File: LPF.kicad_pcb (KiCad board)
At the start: 4 copper layers, 100 x 100 mm, 139 parts, among them J1 Conn_02x05_Counter_Clockwise, P1 SMA, P3 SMA, P4 SMA

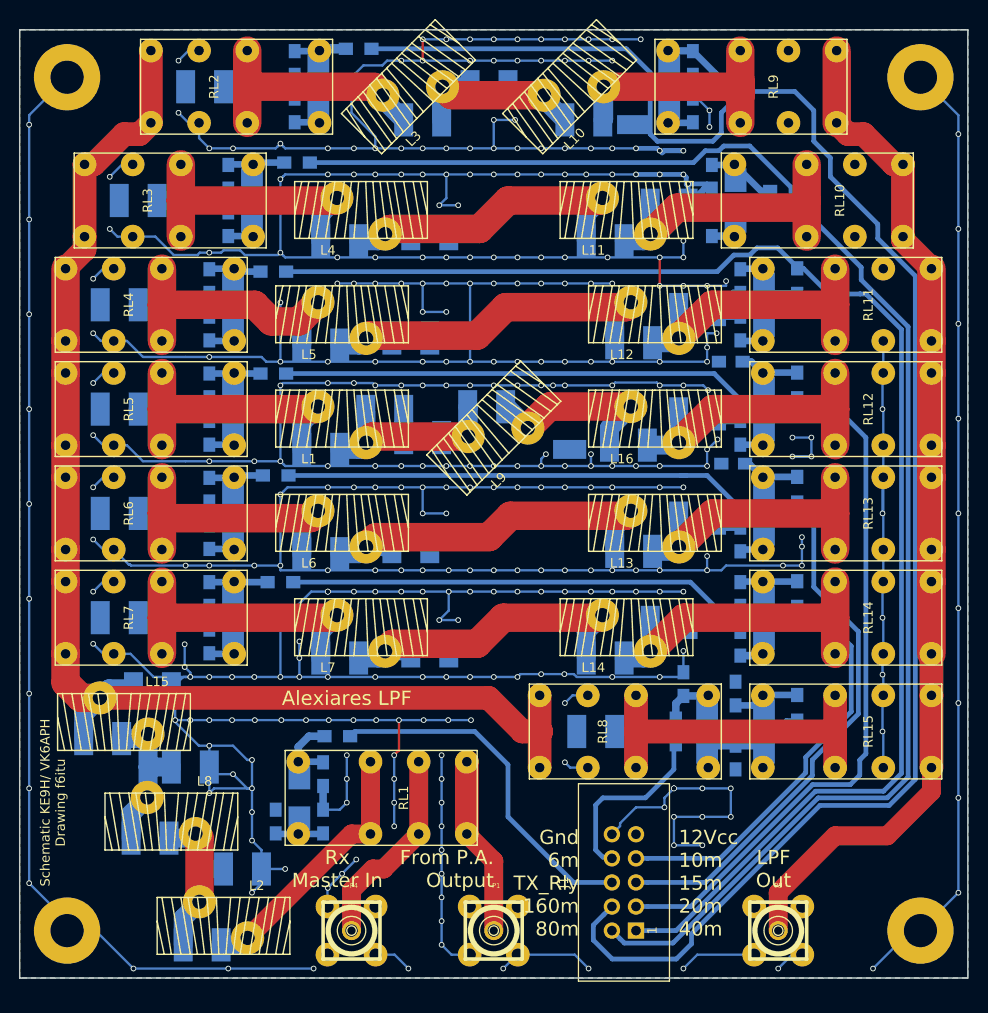
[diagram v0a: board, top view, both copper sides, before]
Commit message: new routing after ATC100B change, RTM2
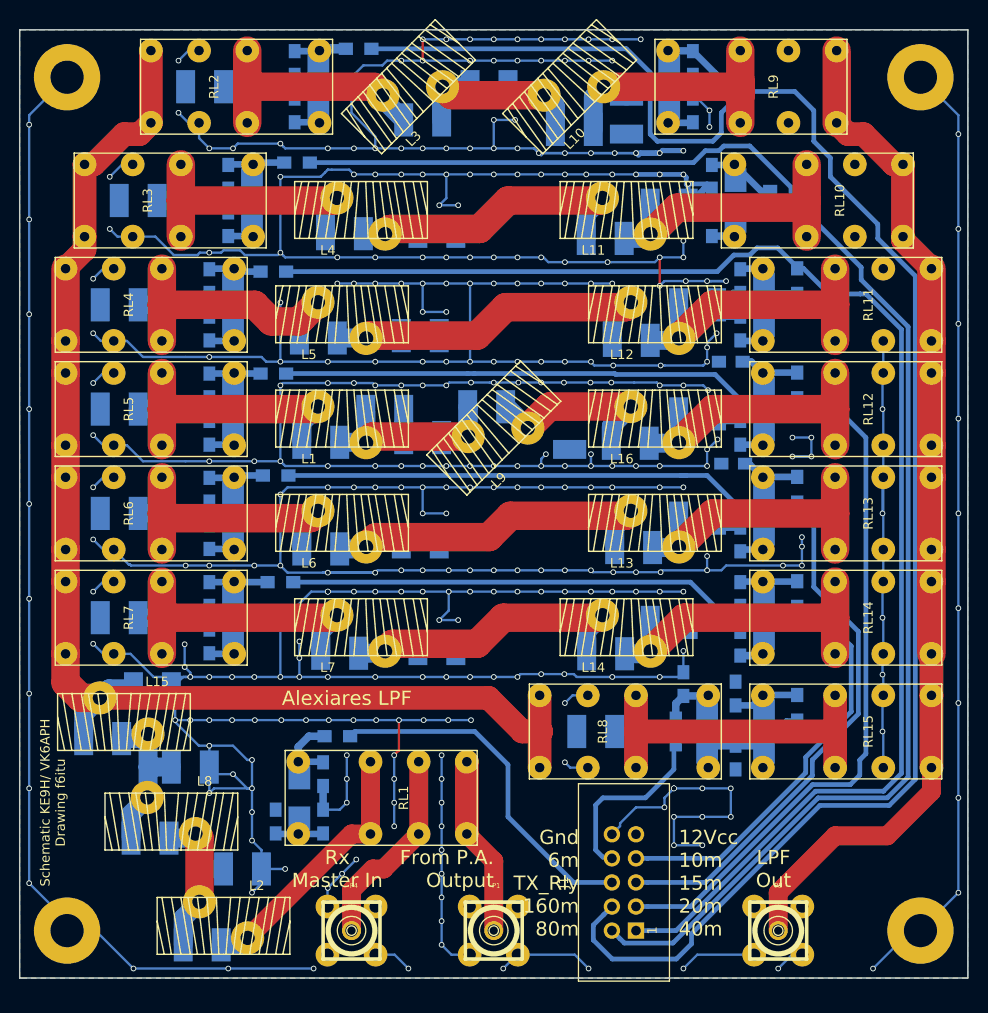
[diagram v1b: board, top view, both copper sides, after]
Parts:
- moved C39 1.41 mm to (113.5, 55.5)
- moved C46 1.25 mm to (119.0, 54.0)
- moved C36 1.12 mm to (97.2, 99.0)
- moved C34 1.03 mm to (97.2, 77.2)
- moved C26 0.90 mm to (89.2, 66.5)
- moved C27 0.79 mm to (86.5, 77.5)
- moved C33 0.79 mm to (99.0, 66.2)
- moved C37 0.79 mm to (99.0, 110.2)
- moved C16 0.75 mm to (86.8, 88.5)
- moved C28 0.50 mm to (86.8, 99.8)
- moved C29 0.50 mm to (88.8, 110.8)
- moved C48 0.50 mm to (126.5, 74.0)
- moved C44 0.45 mm to (116.8, 110.8)
- moved C43 0.40 mm to (119.8, 99.6)
- moved C41 0.35 mm to (119.5, 77.8)
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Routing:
- net 160m: track 166.6 -> 181.3 mm
- net GND: track 1308.3 -> 1313.1 mm, vias 338 -> 337
- net Net-(C27-Pad2): track 40.3 -> 41.6 mm
- net Net-(C39-Pad2): track 30.6 -> 31.7 mm
- net Net-(C20-Pad2): track 39.5 -> 38.6 mm
- net Net-(C51-Pad2): track 32.7 -> 31.8 mm
- net Net-(C43-Pad2): track 32.2 -> 31.4 mm
- net Net-(C11-Pad2): track 39.5 -> 38.8 mm
- net Net-(C28-Pad2): track 40.3 -> 41.0 mm
- net Net-(C41-Pad2): track 31.6 -> 32.3 mm
- net Net-(C21-Pad2): track 41.1 -> 40.4 mm
- net Net-(C25-Pad2): track 21.0 -> 21.6 mm
- net Net-(C23-Pad2): track 41.6 -> 41.1 mm
- net Net-(C22-Pad2): track 40.1 -> 39.6 mm

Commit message: minor routing changes, via added
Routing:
- added copper zone on In2.Cu, net +12V
- added copper zone on In1.Cu, net GND
- removed copper zone on In1.Cu, net +12V
- removed copper zone on In2.Cu, net GND

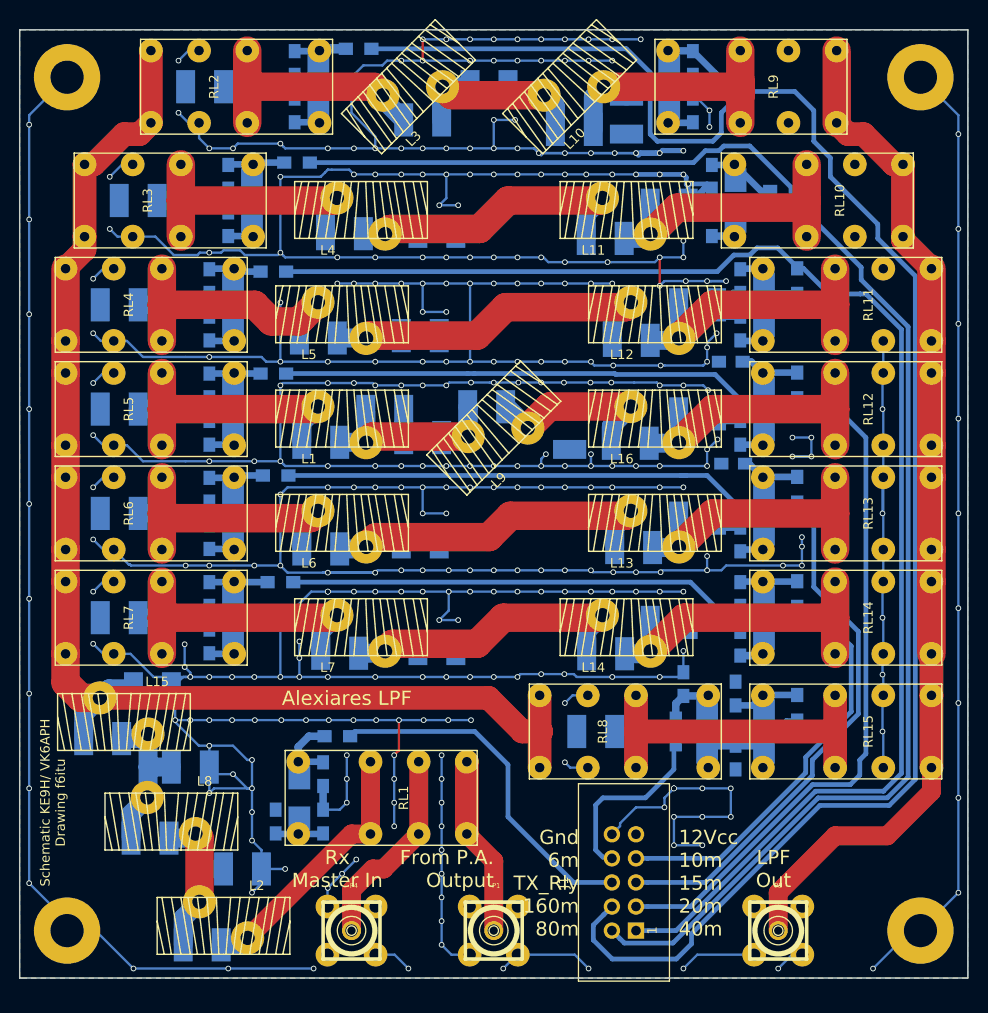
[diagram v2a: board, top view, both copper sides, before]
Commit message: add forbiden zone under bypass power caps
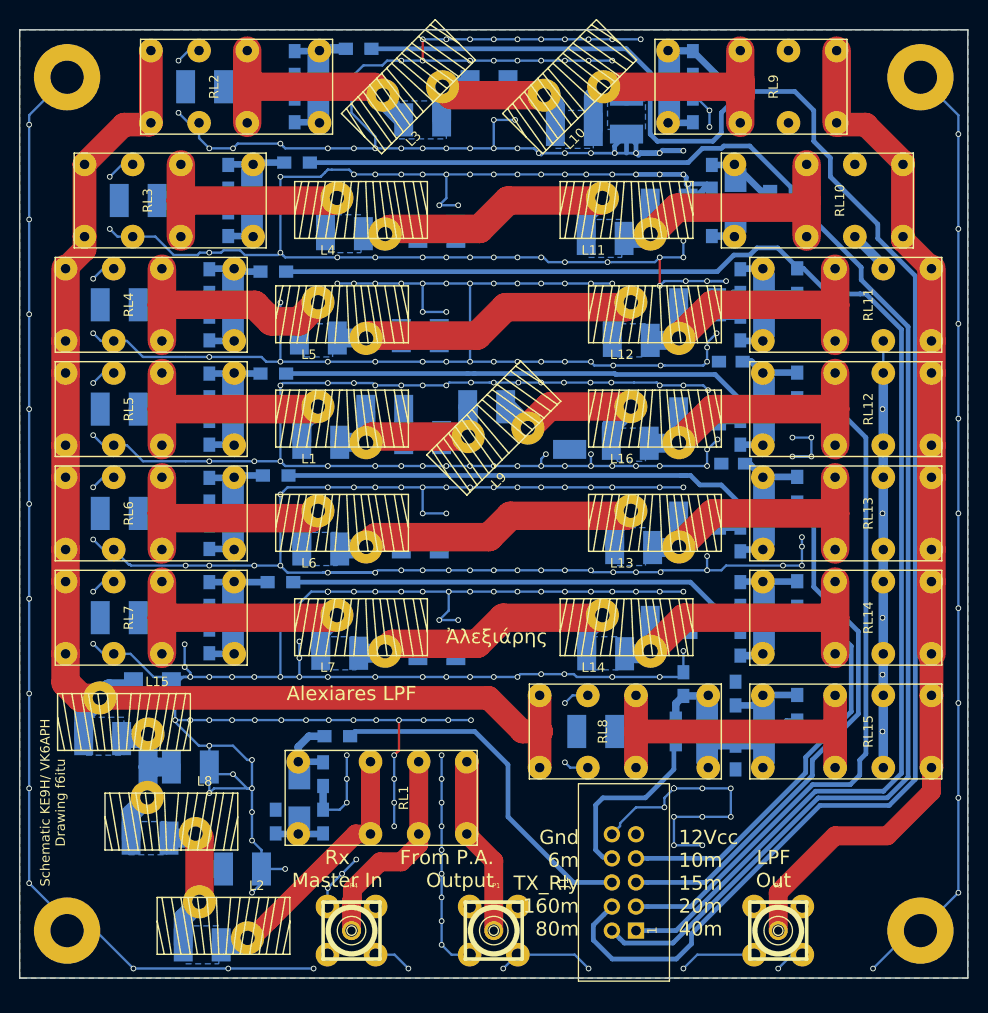
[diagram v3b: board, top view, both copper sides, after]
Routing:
- net GND: track 1313.1 -> 1404.0 mm
- net Net-(C17-Pad1): track 28.2 -> 31.9 mm
- net Net-(P4-Pad1): track 21.4 -> 22.1 mm
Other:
- board text added: "Ἀλεξιάρης"

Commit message: trace cleaning, SMA edge added, main connector rotated
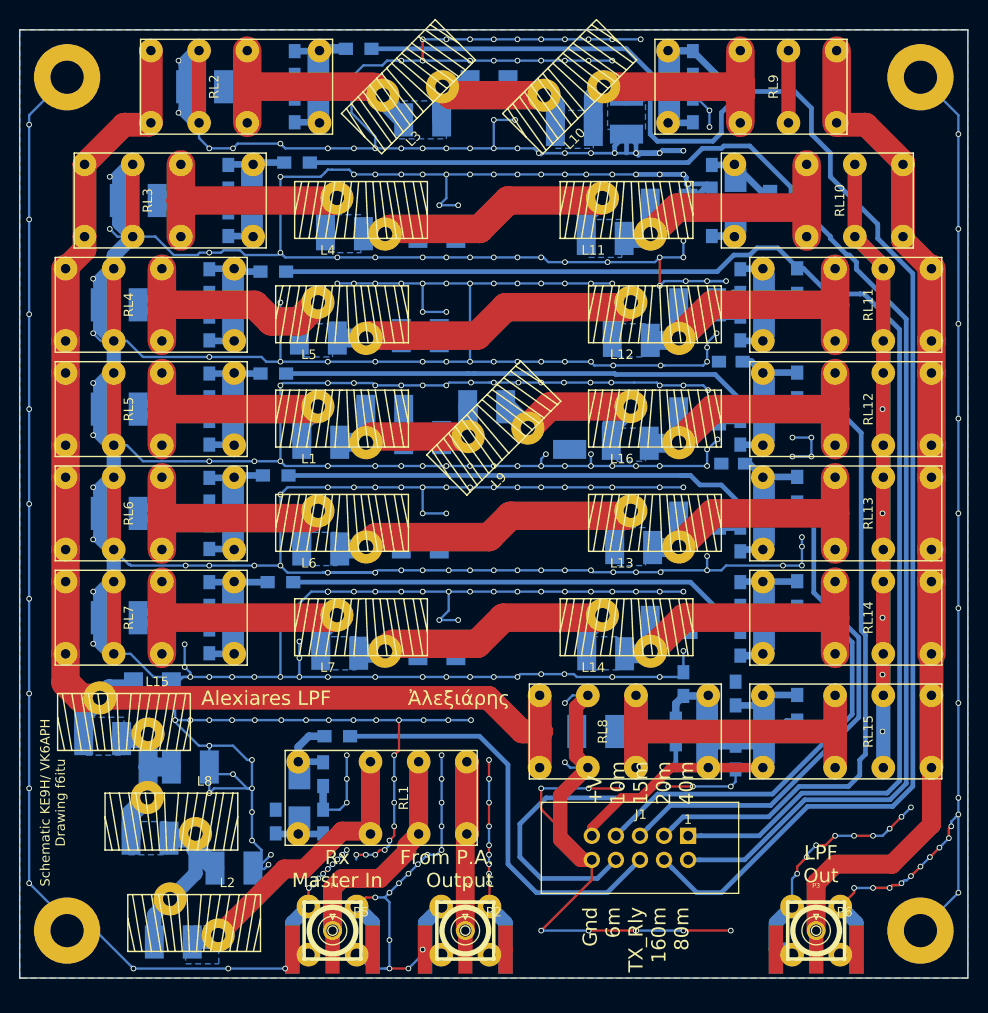
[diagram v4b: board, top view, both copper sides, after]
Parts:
- added P2: SMA, Connector_Coaxial:SMA_Amphenol_132289_EdgeMount, F.Cu at (102.0, 142.0)
- added P5: SMA, Connector_Coaxial:SMA_Amphenol_132289_EdgeMount, F.Cu at (88.0, 142.0)
- added P6: SMA, Connector_Coaxial:SMA_Amphenol_132289_EdgeMount, F.Cu at (139.0, 142.0)
- moved J1 11.4 mm to (125.5, 130.0), turned to 180 degrees
- moved P3 4.00 mm to (139.0, 140.0)
- moved L2 3.11 mm to (73.4, 139.2)
- moved C17 3.06 mm to (71.2, 141.2)
- moved P1 3.00 mm to (102.0, 140.0)
- moved P4 2.00 mm to (88.0, 140.0)
- moved C24 0.91 mm to (77.6, 133.4)
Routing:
- net GND: track 1404.0 -> 1722.1 mm, vias 337 -> 379
- net +12V: track 70.2 -> 91.7 mm
- net 6m_Bypass: track 33.1 -> 50.6 mm
- net 160m: track 181.3 -> 166.7 mm
- net 80m: track 159.7 -> 147.7 mm
- net 40m: track 151.2 -> 141.7 mm
- net TX_RX_RLY: track 37.6 -> 45.0 mm
- net 30/20m: track 130.3 -> 124.2 mm
- net Net-(C17-Pad2): track 25.9 -> 20.7 mm
- net Net-(P4-Pad1): track 22.1 -> 25.9 mm
- net 17/15m: track 113.3 -> 110.1 mm
- net 12/10m: track 99.7 -> 100.5 mm
- net Net-(P1-Pad1): track 19.2 -> 19.9 mm
- net Net-(P3-Pad1): track 108.6 -> 109.2 mm
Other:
- board text added: "+V 10m 15m 20m 40m"
- board text added: "12 Vcc 10m 15m 20m 40m"
- board text added: "Gnd 6m-BP TX_Rly 160m 80m"
- board text removed: "12Vcc 10m 15m 20m 40m"
- board text removed: "Gnd 6m-ByPass TX_Rly 160m 80m"

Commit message: changed sma footprint, gerber done
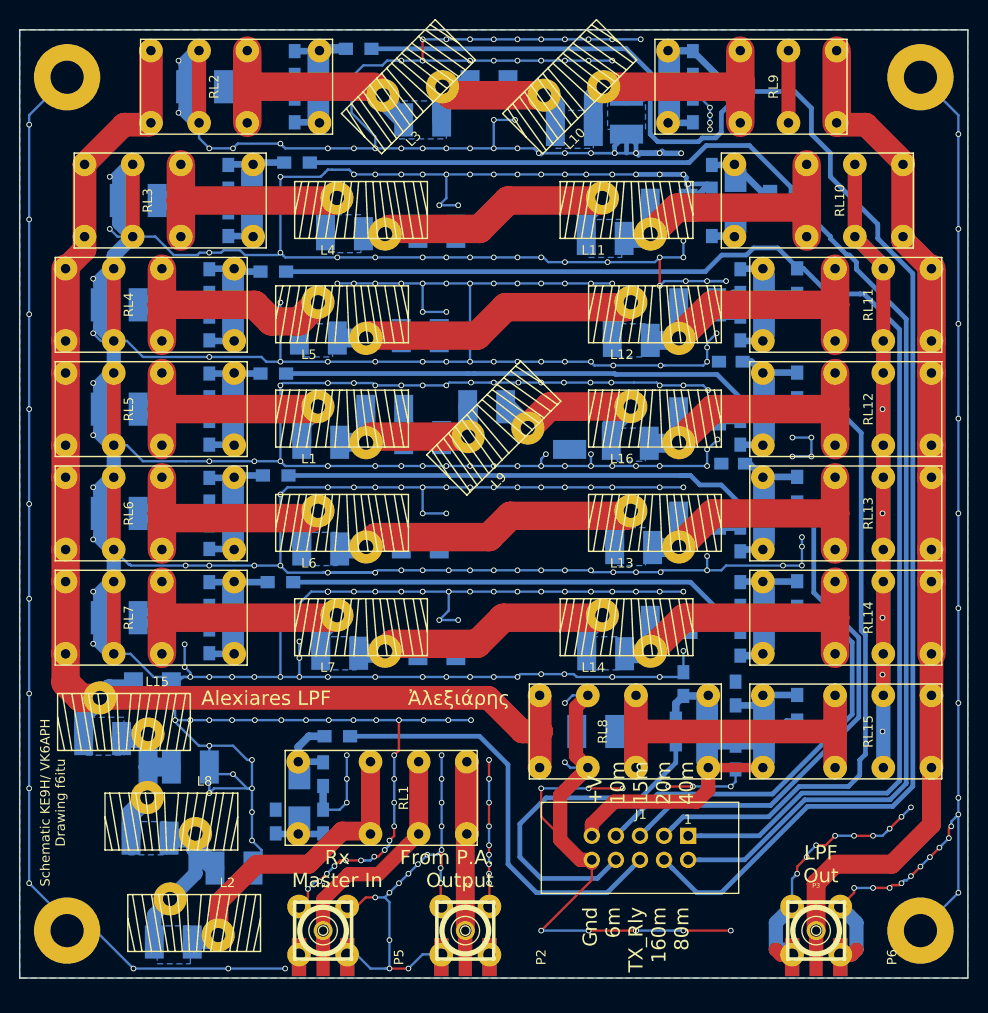
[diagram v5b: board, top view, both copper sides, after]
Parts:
- P2, P5, P6: footprint Connector_Coaxial:SMA_Amphenol_132289_EdgeMount -> SMA_PINS:SMA_EDGE_NRW
- moved P5 1.28 mm to (87.0, 142.8)
- moved P4 1.00 mm to (87.0, 140.0)
- moved P2 0.80 mm to (102.0, 142.8)
- moved P6 0.80 mm to (139.0, 142.8)
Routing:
- net GND: track 1722.1 -> 1697.0 mm, vias 379 -> 375
- net Net-(C17-Pad1): track 31.6 -> 33.6 mm
- net +12V: track 91.7 -> 93.3 mm

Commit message: stitching and new gerber
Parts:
- added REF**: via, via:via, F.Cu at (134.0, 144.0)
- added REF**: via, via:via, F.Cu at (125.0, 144.0)
- added REF**: via, via:via, F.Cu at (119.0, 141.0)
- added REF**: via, via:via, F.Cu at (118.0, 141.0)
- added REF**: via, via:via, F.Cu at (117.0, 141.0)
- added REF**: via, via:via, F.Cu at (116.0, 141.0)
- added REF**: via, via:via, F.Cu at (115.0, 141.0)
- added REF**: via, via:via, F.Cu at (114.0, 141.0)
- added REF**: via, via:via, F.Cu at (113.0, 141.0)
- added REF**: via, via:via, F.Cu at (112.0, 141.0)
- added REF**: via, via:via, F.Cu at (111.0, 141.0)
- added REF**: via, via:via, F.Cu at (110.0, 141.0)
- added REF**: via, via:via, F.Cu at (124.0, 144.0)
- added REF**: via, via:via, F.Cu at (109.0, 141.0)
- added REF**: via, via:via, F.Cu at (108.0, 141.0)
- added REF**: via, via:via, F.Cu at (107.0, 141.0)
- added REF**: via, via:via, F.Cu at (134.0, 140.0)
- added REF**: via, via:via, F.Cu at (133.0, 140.0)
- added REF**: via, via:via, F.Cu at (132.0, 140.0)
- added REF**: via, via:via, F.Cu at (131.0, 140.0)
- added REF**: via, via:via, F.Cu at (130.0, 140.0)
- added REF**: via, via:via, F.Cu at (129.0, 140.0)
- added REF**: via, via:via, F.Cu at (128.0, 140.0)
- added REF**: via, via:via, F.Cu at (123.0, 144.0)
- added REF**: via, via:via, F.Cu at (127.0, 140.0)
- added REF**: via, via:via, F.Cu at (126.0, 140.0)
- added REF**: via, via:via, F.Cu at (125.0, 140.0)
- added REF**: via, via:via, F.Cu at (124.0, 140.0)
- added REF**: via, via:via, F.Cu at (123.0, 140.0)
- added REF**: via, via:via, F.Cu at (122.0, 140.0)
- added REF**: via, via:via, F.Cu at (121.0, 140.0)
- added REF**: via, via:via, F.Cu at (120.0, 140.0)
- added REF**: via, via:via, F.Cu at (119.0, 140.0)
- added REF**: via, via:via, F.Cu at (118.0, 140.0)
- added REF**: via, via:via, F.Cu at (122.0, 144.0)
- added REF**: via, via:via, F.Cu at (117.0, 140.0)
- added REF**: via, via:via, F.Cu at (116.0, 140.0)
- added REF**: via, via:via, F.Cu at (115.0, 140.0)
- added REF**: via, via:via, F.Cu at (114.0, 140.0)
- added REF**: via, via:via, F.Cu at (113.0, 140.0)
- added REF**: via, via:via, F.Cu at (112.0, 140.0)
- added REF**: via, via:via, F.Cu at (111.0, 140.0)
- added REF**: via, via:via, F.Cu at (110.0, 140.0)
- added REF**: via, via:via, F.Cu at (109.0, 140.0)
- added REF**: via, via:via, F.Cu at (108.0, 140.0)
- added REF**: via, via:via, F.Cu at (121.0, 144.0)
- added REF**: via, via:via, F.Cu at (107.0, 140.0)
- added REF**: via, via:via, F.Cu at (134.0, 139.0)
- added REF**: via, via:via, F.Cu at (133.0, 139.0)
- added REF**: via, via:via, F.Cu at (132.0, 139.0)
- added REF**: via, via:via, F.Cu at (131.0, 139.0)
- added REF**: via, via:via, F.Cu at (130.0, 139.0)
- added REF**: via, via:via, F.Cu at (129.0, 139.0)
- added REF**: via, via:via, F.Cu at (128.0, 139.0)
- added REF**: via, via:via, F.Cu at (127.0, 139.0)
- added REF**: via, via:via, F.Cu at (126.0, 139.0)
- added REF**: via, via:via, F.Cu at (120.0, 144.0)
- added REF**: via, via:via, F.Cu at (125.0, 139.0)
- added REF**: via, via:via, F.Cu at (124.0, 139.0)
- added REF**: via, via:via, F.Cu at (123.0, 139.0)
- added REF**: via, via:via, F.Cu at (122.0, 139.0)
- added REF**: via, via:via, F.Cu at (121.0, 139.0)
- added REF**: via, via:via, F.Cu at (120.0, 139.0)
- added REF**: via, via:via, F.Cu at (119.0, 139.0)
- added REF**: via, via:via, F.Cu at (118.0, 139.0)
- added REF**: via, via:via, F.Cu at (117.0, 139.0)
- added REF**: via, via:via, F.Cu at (116.0, 139.0)
- added REF**: via, via:via, F.Cu at (119.0, 144.0)
- added REF**: via, via:via, F.Cu at (115.0, 139.0)
- added REF**: via, via:via, F.Cu at (114.0, 139.0)
- added REF**: via, via:via, F.Cu at (113.0, 139.0)
- added REF**: via, via:via, F.Cu at (112.0, 139.0)
- added REF**: via, via:via, F.Cu at (111.0, 139.0)
- added REF**: via, via:via, F.Cu at (110.0, 139.0)
- added REF**: via, via:via, F.Cu at (109.0, 139.0)
- added REF**: via, via:via, F.Cu at (108.0, 139.0)
- added REF**: via, via:via, F.Cu at (107.0, 139.0)
- added REF**: via, via:via, F.Cu at (134.0, 138.0)
- added REF**: via, via:via, F.Cu at (118.0, 144.0)
- added REF**: via, via:via, F.Cu at (133.0, 138.0)
- added REF**: via, via:via, F.Cu at (132.0, 138.0)
- added REF**: via, via:via, F.Cu at (131.0, 138.0)
- added REF**: via, via:via, F.Cu at (130.0, 138.0)
- added REF**: via, via:via, F.Cu at (129.0, 138.0)
- added REF**: via, via:via, F.Cu at (128.0, 138.0)
- added REF**: via, via:via, F.Cu at (127.0, 138.0)
- added REF**: via, via:via, F.Cu at (126.0, 138.0)
- added REF**: via, via:via, F.Cu at (125.0, 138.0)
- added REF**: via, via:via, F.Cu at (124.0, 138.0)
- added REF**: via, via:via, F.Cu at (117.0, 144.0)
- added REF**: via, via:via, F.Cu at (123.0, 138.0)
- added REF**: via, via:via, F.Cu at (122.0, 138.0)
- added REF**: via, via:via, F.Cu at (121.0, 138.0)
- added REF**: via, via:via, F.Cu at (120.0, 138.0)
- added REF**: via, via:via, F.Cu at (119.0, 138.0)
- added REF**: via, via:via, F.Cu at (118.0, 138.0)
- added REF**: via, via:via, F.Cu at (117.0, 138.0)
- added REF**: via, via:via, F.Cu at (116.0, 138.0)
- added REF**: via, via:via, F.Cu at (115.0, 138.0)
- added REF**: via, via:via, F.Cu at (114.0, 138.0)
- added REF**: via, via:via, F.Cu at (116.0, 144.0)
- added REF**: via, via:via, F.Cu at (113.0, 138.0)
- added REF**: via, via:via, F.Cu at (112.0, 138.0)
- added REF**: via, via:via, F.Cu at (111.0, 138.0)
- added REF**: via, via:via, F.Cu at (110.0, 138.0)
- added REF**: via, via:via, F.Cu at (109.0, 138.0)
- added REF**: via, via:via, F.Cu at (108.0, 138.0)
- added REF**: via, via:via, F.Cu at (107.0, 138.0)
- added REF**: via, via:via, F.Cu at (154.0, 136.0)
- added REF**: via, via:via, F.Cu at (154.0, 135.0)
- added REF**: via, via:via, F.Cu at (154.0, 134.0)
- added REF**: via, via:via, F.Cu at (133.0, 144.0)
- added REF**: via, via:via, F.Cu at (115.0, 144.0)
- added REF**: via, via:via, F.Cu at (154.0, 133.0)
- added REF**: via, via:via, F.Cu at (154.0, 132.0)
- added REF**: via, via:via, F.Cu at (154.0, 131.0)
- added REF**: via, via:via, F.Cu at (154.0, 130.0)
- added REF**: via, via:via, F.Cu at (154.0, 129.0)
- added REF**: via, via:via, F.Cu at (154.0, 128.0)
- added REF**: via, via:via, F.Cu at (154.0, 127.0)
- added REF**: via, via:via, F.Cu at (154.0, 126.0)
- added REF**: via, via:via, F.Cu at (154.0, 125.0)
- added REF**: via, via:via, F.Cu at (154.0, 124.0)
- added REF**: via, via:via, F.Cu at (114.0, 144.0)
- added REF**: via, via:via, F.Cu at (154.0, 123.0)
- added REF**: via, via:via, F.Cu at (154.0, 122.0)
- added REF**: via, via:via, F.Cu at (154.0, 121.0)
- added REF**: via, via:via, F.Cu at (154.0, 120.0)
- added REF**: via, via:via, F.Cu at (154.0, 119.0)
- added REF**: via, via:via, F.Cu at (154.0, 118.0)
- added REF**: via, via:via, F.Cu at (154.0, 117.0)
- added REF**: via, via:via, F.Cu at (154.0, 116.0)
- added REF**: via, via:via, F.Cu at (154.0, 115.0)
- added REF**: via, via:via, F.Cu at (154.0, 114.0)
- added REF**: via, via:via, F.Cu at (113.0, 144.0)
- added REF**: via, via:via, F.Cu at (154.0, 113.0)
- added REF**: via, via:via, F.Cu at (154.0, 112.0)
- added REF**: via, via:via, F.Cu at (154.0, 111.0)
- added REF**: via, via:via, F.Cu at (154.0, 110.0)
- added REF**: via, via:via, F.Cu at (154.0, 109.0)
- added REF**: via, via:via, F.Cu at (154.0, 108.0)
- added REF**: via, via:via, F.Cu at (154.0, 107.0)
- added REF**: via, via:via, F.Cu at (154.0, 106.0)
- added REF**: via, via:via, F.Cu at (154.0, 105.0)
- added REF**: via, via:via, F.Cu at (154.0, 104.0)
- added REF**: via, via:via, F.Cu at (112.0, 144.0)
- added REF**: via, via:via, F.Cu at (154.0, 103.0)
- added REF**: via, via:via, F.Cu at (154.0, 102.0)
- added REF**: via, via:via, F.Cu at (154.0, 101.0)
- added REF**: via, via:via, F.Cu at (154.0, 100.0)
- added REF**: via, via:via, F.Cu at (154.0, 99.0)
- added REF**: via, via:via, F.Cu at (154.0, 98.0)
- added REF**: via, via:via, F.Cu at (154.0, 97.0)
- added REF**: via, via:via, F.Cu at (154.0, 96.0)
- added REF**: via, via:via, F.Cu at (154.0, 95.0)
- added REF**: via, via:via, F.Cu at (154.0, 94.0)
- added REF**: via, via:via, F.Cu at (111.0, 144.0)
- added REF**: via, via:via, F.Cu at (154.0, 93.0)
- added REF**: via, via:via, F.Cu at (154.0, 92.0)
- added REF**: via, via:via, F.Cu at (154.0, 91.0)
- added REF**: via, via:via, F.Cu at (154.0, 90.0)
- added REF**: via, via:via, F.Cu at (154.0, 89.0)
- added REF**: via, via:via, F.Cu at (154.0, 88.0)
- added REF**: via, via:via, F.Cu at (154.0, 87.0)
- added REF**: via, via:via, F.Cu at (154.0, 86.0)
- added REF**: via, via:via, F.Cu at (154.0, 85.0)
- added REF**: via, via:via, F.Cu at (154.0, 84.0)
- added REF**: via, via:via, F.Cu at (110.0, 144.0)
- added REF**: via, via:via, F.Cu at (154.0, 83.0)
- added REF**: via, via:via, F.Cu at (154.0, 82.0)
- added REF**: via, via:via, F.Cu at (154.0, 81.0)
- added REF**: via, via:via, F.Cu at (154.0, 80.0)
- added REF**: via, via:via, F.Cu at (154.0, 79.0)
- added REF**: via, via:via, F.Cu at (154.0, 78.0)
- added REF**: via, via:via, F.Cu at (154.0, 77.0)
- added REF**: via, via:via, F.Cu at (154.0, 76.0)
- added REF**: via, via:via, F.Cu at (154.0, 75.0)
- added REF**: via, via:via, F.Cu at (154.0, 74.0)
- added REF**: via, via:via, F.Cu at (109.0, 144.0)
- added REF**: via, via:via, F.Cu at (154.0, 73.0)
- added REF**: via, via:via, F.Cu at (154.0, 72.0)
- added REF**: via, via:via, F.Cu at (154.0, 71.0)
- added REF**: via, via:via, F.Cu at (154.0, 70.0)
- added REF**: via, via:via, F.Cu at (154.0, 69.0)
- added REF**: via, via:via, F.Cu at (154.0, 68.0)
- added REF**: via, via:via, F.Cu at (154.0, 67.0)
- added REF**: via, via:via, F.Cu at (154.0, 66.0)
- added REF**: via, via:via, F.Cu at (154.0, 65.0)
- added REF**: via, via:via, F.Cu at (154.0, 64.0)
- added REF**: via, via:via, F.Cu at (108.0, 144.0)
- added REF**: via, via:via, F.Cu at (154.0, 63.0)
- added REF**: via, via:via, F.Cu at (154.0, 62.0)
- added REF**: via, via:via, F.Cu at (154.0, 61.0)
- added REF**: via, via:via, F.Cu at (154.0, 60.0)
- added REF**: via, via:via, F.Cu at (154.0, 59.0)
- added REF**: via, via:via, F.Cu at (154.0, 58.0)
- added REF**: via, via:via, F.Cu at (154.0, 57.0)
- added REF**: via, via:via, F.Cu at (154.0, 56.0)
- added REF**: via, via:via, F.Cu at (154.0, 55.0)
- added REF**: via, via:via, F.Cu at (154.0, 54.0)
- added REF**: via, via:via, F.Cu at (107.0, 144.0)
- added REF**: via, via:via, F.Cu at (57.0, 136.0)
- added REF**: via, via:via, F.Cu at (56.0, 136.0)
- added REF**: via, via:via, F.Cu at (57.0, 135.0)
- added REF**: via, via:via, F.Cu at (56.0, 135.0)
- added REF**: via, via:via, F.Cu at (57.0, 134.0)
- added REF**: via, via:via, F.Cu at (56.0, 134.0)
- added REF**: via, via:via, F.Cu at (57.0, 133.0)
- added REF**: via, via:via, F.Cu at (56.0, 133.0)
- added REF**: via, via:via, F.Cu at (57.0, 132.0)
- added REF**: via, via:via, F.Cu at (56.0, 132.0)
- added REF**: via, via:via, F.Cu at (134.0, 143.0)
- added REF**: via, via:via, F.Cu at (57.0, 131.0)
- added REF**: via, via:via, F.Cu at (56.0, 131.0)
- added REF**: via, via:via, F.Cu at (57.0, 130.0)
- added REF**: via, via:via, F.Cu at (56.0, 130.0)
- added REF**: via, via:via, F.Cu at (57.0, 129.0)
- added REF**: via, via:via, F.Cu at (56.0, 129.0)
- added REF**: via, via:via, F.Cu at (57.0, 128.0)
- added REF**: via, via:via, F.Cu at (56.0, 128.0)
- added REF**: via, via:via, F.Cu at (57.0, 127.0)
- added REF**: via, via:via, F.Cu at (56.0, 127.0)
- added REF**: via, via:via, F.Cu at (132.0, 144.0)
- added REF**: via, via:via, F.Cu at (133.0, 143.0)
- added REF**: via, via:via, F.Cu at (57.0, 126.0)
- added REF**: via, via:via, F.Cu at (56.0, 126.0)
- added REF**: via, via:via, F.Cu at (57.0, 125.0)
- added REF**: via, via:via, F.Cu at (56.0, 125.0)
- added REF**: via, via:via, F.Cu at (57.0, 124.0)
- added REF**: via, via:via, F.Cu at (56.0, 124.0)
- added REF**: via, via:via, F.Cu at (57.0, 123.0)
- added REF**: via, via:via, F.Cu at (56.0, 123.0)
- added REF**: via, via:via, F.Cu at (57.0, 122.0)
- added REF**: via, via:via, F.Cu at (56.0, 122.0)
- added REF**: via, via:via, F.Cu at (132.0, 143.0)
- added REF**: via, via:via, F.Cu at (57.0, 121.0)
- added REF**: via, via:via, F.Cu at (56.0, 121.0)
- added REF**: via, via:via, F.Cu at (57.0, 120.0)
- added REF**: via, via:via, F.Cu at (56.0, 120.0)
- added REF**: via, via:via, F.Cu at (57.0, 119.0)
- added REF**: via, via:via, F.Cu at (56.0, 119.0)
- added REF**: via, via:via, F.Cu at (57.0, 118.0)
- added REF**: via, via:via, F.Cu at (56.0, 118.0)
- added REF**: via, via:via, F.Cu at (57.0, 117.0)
- added REF**: via, via:via, F.Cu at (56.0, 117.0)
- added REF**: via, via:via, F.Cu at (131.0, 143.0)
- added REF**: via, via:via, F.Cu at (57.0, 116.0)
- added REF**: via, via:via, F.Cu at (56.0, 116.0)
- added REF**: via, via:via, F.Cu at (57.0, 115.0)
- added REF**: via, via:via, F.Cu at (56.0, 115.0)
- added REF**: via, via:via, F.Cu at (57.0, 114.0)
- added REF**: via, via:via, F.Cu at (56.0, 114.0)
- added REF**: via, via:via, F.Cu at (57.0, 113.0)
- added REF**: via, via:via, F.Cu at (56.0, 113.0)
- added REF**: via, via:via, F.Cu at (57.0, 112.0)
- added REF**: via, via:via, F.Cu at (56.0, 112.0)
- added REF**: via, via:via, F.Cu at (130.0, 143.0)
- added REF**: via, via:via, F.Cu at (57.0, 111.0)
- added REF**: via, via:via, F.Cu at (56.0, 111.0)
- added REF**: via, via:via, F.Cu at (57.0, 110.0)
- added REF**: via, via:via, F.Cu at (56.0, 110.0)
- added REF**: via, via:via, F.Cu at (57.0, 109.0)
- added REF**: via, via:via, F.Cu at (56.0, 109.0)
- added REF**: via, via:via, F.Cu at (57.0, 108.0)
- added REF**: via, via:via, F.Cu at (56.0, 108.0)
- added REF**: via, via:via, F.Cu at (57.0, 107.0)
- added REF**: via, via:via, F.Cu at (56.0, 107.0)
- added REF**: via, via:via, F.Cu at (129.0, 143.0)
- added REF**: via, via:via, F.Cu at (57.0, 106.0)
- added REF**: via, via:via, F.Cu at (56.0, 106.0)
- added REF**: via, via:via, F.Cu at (57.0, 105.0)
- added REF**: via, via:via, F.Cu at (56.0, 105.0)
- added REF**: via, via:via, F.Cu at (57.0, 104.0)
- added REF**: via, via:via, F.Cu at (56.0, 104.0)
- added REF**: via, via:via, F.Cu at (57.0, 103.0)
- added REF**: via, via:via, F.Cu at (56.0, 103.0)
- added REF**: via, via:via, F.Cu at (57.0, 102.0)
- added REF**: via, via:via, F.Cu at (56.0, 102.0)
- added REF**: via, via:via, F.Cu at (128.0, 143.0)
- added REF**: via, via:via, F.Cu at (57.0, 101.0)
- added REF**: via, via:via, F.Cu at (56.0, 101.0)
- added REF**: via, via:via, F.Cu at (57.0, 100.0)
- added REF**: via, via:via, F.Cu at (56.0, 100.0)
- added REF**: via, via:via, F.Cu at (57.0, 99.0)
- added REF**: via, via:via, F.Cu at (56.0, 99.0)
- added REF**: via, via:via, F.Cu at (57.0, 98.0)
- added REF**: via, via:via, F.Cu at (56.0, 98.0)
- added REF**: via, via:via, F.Cu at (57.0, 97.0)
- added REF**: via, via:via, F.Cu at (56.0, 97.0)
- added REF**: via, via:via, F.Cu at (127.0, 143.0)
- added REF**: via, via:via, F.Cu at (57.0, 96.0)
- added REF**: via, via:via, F.Cu at (56.0, 96.0)
- added REF**: via, via:via, F.Cu at (57.0, 95.0)
- added REF**: via, via:via, F.Cu at (56.0, 95.0)
- added REF**: via, via:via, F.Cu at (57.0, 94.0)
- added REF**: via, via:via, F.Cu at (56.0, 94.0)
- added REF**: via, via:via, F.Cu at (57.0, 93.0)
- added REF**: via, via:via, F.Cu at (56.0, 93.0)
- added REF**: via, via:via, F.Cu at (57.0, 92.0)
- added REF**: via, via:via, F.Cu at (56.0, 92.0)
- added REF**: via, via:via, F.Cu at (126.0, 143.0)
- added REF**: via, via:via, F.Cu at (57.0, 91.0)
- added REF**: via, via:via, F.Cu at (56.0, 91.0)
- added REF**: via, via:via, F.Cu at (57.0, 90.0)
- added REF**: via, via:via, F.Cu at (56.0, 90.0)
- added REF**: via, via:via, F.Cu at (57.0, 89.0)
- added REF**: via, via:via, F.Cu at (56.0, 89.0)
- added REF**: via, via:via, F.Cu at (57.0, 88.0)
- added REF**: via, via:via, F.Cu at (56.0, 88.0)
- added REF**: via, via:via, F.Cu at (57.0, 87.0)
- added REF**: via, via:via, F.Cu at (56.0, 87.0)
- added REF**: via, via:via, F.Cu at (125.0, 143.0)
- added REF**: via, via:via, F.Cu at (57.0, 86.0)
- added REF**: via, via:via, F.Cu at (56.0, 86.0)
- added REF**: via, via:via, F.Cu at (57.0, 85.0)
- added REF**: via, via:via, F.Cu at (56.0, 85.0)
- added REF**: via, via:via, F.Cu at (57.0, 84.0)
- added REF**: via, via:via, F.Cu at (56.0, 84.0)
- added REF**: via, via:via, F.Cu at (57.0, 83.0)
- added REF**: via, via:via, F.Cu at (56.0, 83.0)
- added REF**: via, via:via, F.Cu at (57.0, 82.0)
- added REF**: via, via:via, F.Cu at (56.0, 82.0)
- added REF**: via, via:via, F.Cu at (124.0, 143.0)
- added REF**: via, via:via, F.Cu at (57.0, 81.0)
- added REF**: via, via:via, F.Cu at (56.0, 81.0)
- added REF**: via, via:via, F.Cu at (57.0, 80.0)
- added REF**: via, via:via, F.Cu at (56.0, 80.0)
- added REF**: via, via:via, F.Cu at (57.0, 79.0)
- added REF**: via, via:via, F.Cu at (56.0, 79.0)
- added REF**: via, via:via, F.Cu at (57.0, 78.0)
- added REF**: via, via:via, F.Cu at (56.0, 78.0)
- added REF**: via, via:via, F.Cu at (57.0, 77.0)
- added REF**: via, via:via, F.Cu at (56.0, 77.0)
- added REF**: via, via:via, F.Cu at (131.0, 144.0)
- added REF**: via, via:via, F.Cu at (123.0, 143.0)
- added REF**: via, via:via, F.Cu at (57.0, 76.0)
- added REF**: via, via:via, F.Cu at (56.0, 76.0)
- added REF**: via, via:via, F.Cu at (57.0, 75.0)
- added REF**: via, via:via, F.Cu at (56.0, 75.0)
- added REF**: via, via:via, F.Cu at (57.0, 74.0)
- added REF**: via, via:via, F.Cu at (56.0, 74.0)
- added REF**: via, via:via, F.Cu at (57.0, 73.0)
- added REF**: via, via:via, F.Cu at (56.0, 73.0)
- added REF**: via, via:via, F.Cu at (57.0, 72.0)
- added REF**: via, via:via, F.Cu at (56.0, 72.0)
- added REF**: via, via:via, F.Cu at (122.0, 143.0)
- added REF**: via, via:via, F.Cu at (57.0, 71.0)
- added REF**: via, via:via, F.Cu at (56.0, 71.0)
- added REF**: via, via:via, F.Cu at (57.0, 70.0)
- added REF**: via, via:via, F.Cu at (56.0, 70.0)
- added REF**: via, via:via, F.Cu at (57.0, 69.0)
- added REF**: via, via:via, F.Cu at (56.0, 69.0)
- added REF**: via, via:via, F.Cu at (57.0, 68.0)
- added REF**: via, via:via, F.Cu at (56.0, 68.0)
- added REF**: via, via:via, F.Cu at (57.0, 67.0)
- added REF**: via, via:via, F.Cu at (56.0, 67.0)
- added REF**: via, via:via, F.Cu at (121.0, 143.0)
- added REF**: via, via:via, F.Cu at (57.0, 66.0)
- added REF**: via, via:via, F.Cu at (56.0, 66.0)
- added REF**: via, via:via, F.Cu at (57.0, 65.0)
- added REF**: via, via:via, F.Cu at (56.0, 65.0)
- added REF**: via, via:via, F.Cu at (57.0, 64.0)
- added REF**: via, via:via, F.Cu at (56.0, 64.0)
- added REF**: via, via:via, F.Cu at (57.0, 63.0)
- added REF**: via, via:via, F.Cu at (56.0, 63.0)
- added REF**: via, via:via, F.Cu at (57.0, 62.0)
- added REF**: via, via:via, F.Cu at (56.0, 62.0)
- added REF**: via, via:via, F.Cu at (120.0, 143.0)
- added REF**: via, via:via, F.Cu at (57.0, 61.0)
- added REF**: via, via:via, F.Cu at (56.0, 61.0)
- added REF**: via, via:via, F.Cu at (57.0, 60.0)
- added REF**: via, via:via, F.Cu at (56.0, 60.0)
- added REF**: via, via:via, F.Cu at (57.0, 59.0)
- added REF**: via, via:via, F.Cu at (56.0, 59.0)
- added REF**: via, via:via, F.Cu at (57.0, 58.0)
- added REF**: via, via:via, F.Cu at (56.0, 58.0)
- added REF**: via, via:via, F.Cu at (57.0, 57.0)
- added REF**: via, via:via, F.Cu at (56.0, 57.0)
- added REF**: via, via:via, F.Cu at (119.0, 143.0)
- added REF**: via, via:via, F.Cu at (57.0, 56.0)
- added REF**: via, via:via, F.Cu at (56.0, 56.0)
- added REF**: via, via:via, F.Cu at (57.0, 55.0)
- added REF**: via, via:via, F.Cu at (56.0, 55.0)
- added REF**: via, via:via, F.Cu at (57.0, 54.0)
- added REF**: via, via:via, F.Cu at (56.0, 54.0)
- added REF**: via, via:via, F.Cu at (118.0, 143.0)
- added REF**: via, via:via, F.Cu at (117.0, 143.0)
- added REF**: via, via:via, F.Cu at (116.0, 143.0)
- added REF**: via, via:via, F.Cu at (115.0, 143.0)
- added REF**: via, via:via, F.Cu at (114.0, 143.0)
- added REF**: via, via:via, F.Cu at (130.0, 144.0)
- added REF**: via, via:via, F.Cu at (113.0, 143.0)
- added REF**: via, via:via, F.Cu at (112.0, 143.0)
- added REF**: via, via:via, F.Cu at (111.0, 143.0)
- added REF**: via, via:via, F.Cu at (110.0, 143.0)
- added REF**: via, via:via, F.Cu at (109.0, 143.0)
- added REF**: via, via:via, F.Cu at (108.0, 143.0)
- added REF**: via, via:via, F.Cu at (107.0, 143.0)
- added REF**: via, via:via, F.Cu at (134.0, 142.0)
- added REF**: via, via:via, F.Cu at (133.0, 142.0)
- added REF**: via, via:via, F.Cu at (132.0, 142.0)
- added REF**: via, via:via, F.Cu at (129.0, 144.0)
- added REF**: via, via:via, F.Cu at (131.0, 142.0)
- added REF**: via, via:via, F.Cu at (130.0, 142.0)
- added REF**: via, via:via, F.Cu at (129.0, 142.0)
- added REF**: via, via:via, F.Cu at (128.0, 142.0)
- added REF**: via, via:via, F.Cu at (127.0, 142.0)
- added REF**: via, via:via, F.Cu at (126.0, 142.0)
- added REF**: via, via:via, F.Cu at (125.0, 142.0)
- added REF**: via, via:via, F.Cu at (124.0, 142.0)
- added REF**: via, via:via, F.Cu at (123.0, 142.0)
- added REF**: via, via:via, F.Cu at (122.0, 142.0)
- added REF**: via, via:via, F.Cu at (128.0, 144.0)
- added REF**: via, via:via, F.Cu at (121.0, 142.0)
- added REF**: via, via:via, F.Cu at (120.0, 142.0)
- added REF**: via, via:via, F.Cu at (119.0, 142.0)
- added REF**: via, via:via, F.Cu at (118.0, 142.0)
- added REF**: via, via:via, F.Cu at (117.0, 142.0)
- added REF**: via, via:via, F.Cu at (116.0, 142.0)
- added REF**: via, via:via, F.Cu at (115.0, 142.0)
- added REF**: via, via:via, F.Cu at (114.0, 142.0)
- added REF**: via, via:via, F.Cu at (113.0, 142.0)
- added REF**: via, via:via, F.Cu at (112.0, 142.0)
- added REF**: via, via:via, F.Cu at (127.0, 144.0)
- added REF**: via, via:via, F.Cu at (111.0, 142.0)
- added REF**: via, via:via, F.Cu at (110.0, 142.0)
- added REF**: via, via:via, F.Cu at (109.0, 142.0)
- added REF**: via, via:via, F.Cu at (108.0, 142.0)
- added REF**: via, via:via, F.Cu at (107.0, 142.0)
- added REF**: via, via:via, F.Cu at (134.0, 141.0)
- added REF**: via, via:via, F.Cu at (133.0, 141.0)
- added REF**: via, via:via, F.Cu at (132.0, 141.0)
- added REF**: via, via:via, F.Cu at (131.0, 141.0)
- added REF**: via, via:via, F.Cu at (130.0, 141.0)
- added REF**: via, via:via, F.Cu at (126.0, 144.0)
- added REF**: via, via:via, F.Cu at (129.0, 141.0)
- added REF**: via, via:via, F.Cu at (128.0, 141.0)
- added REF**: via, via:via, F.Cu at (127.0, 141.0)
- added REF**: via, via:via, F.Cu at (126.0, 141.0)
- added REF**: via, via:via, F.Cu at (125.0, 141.0)
- added REF**: via, via:via, F.Cu at (124.0, 141.0)
- added REF**: via, via:via, F.Cu at (123.0, 141.0)
- added REF**: via, via:via, F.Cu at (122.0, 141.0)
- added REF**: via, via:via, F.Cu at (121.0, 141.0)
- added REF**: via, via:via, F.Cu at (120.0, 141.0)
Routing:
- net GND: track 1697.0 -> 1437.5 mm, vias 375 -> 595
- net Net-(C45-Pad2): track 140.9 -> 146.2 mm, vias 0 -> 3
- net (no net): track 0.00 -> 3.50 mm, vias 0 -> 3

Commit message: new stitching, new gerber
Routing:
- net GND: track 1437.5 -> 1399.5 mm, vias 595 -> 640
- net (no net): track 3.50 -> 25.3 mm, vias 3 -> 17
- net Net-(C45-Pad2): track 146.2 -> 140.9 mm, vias 3 -> 0
